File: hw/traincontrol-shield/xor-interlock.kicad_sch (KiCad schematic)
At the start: 4 parts, among them U3 74LVC1G86, U4 74LVC2G08

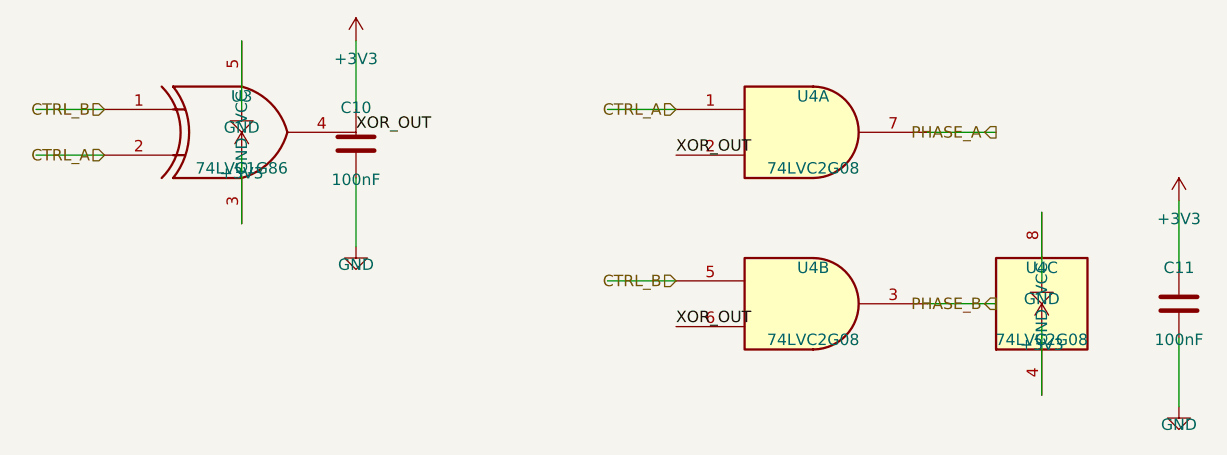
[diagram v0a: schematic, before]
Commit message: Revert "Fix hierarchical label orientations: angle=0 → angle=180 throughout"
This reverts commit 593a08d7401abe541600d63447176c71f07219f1.
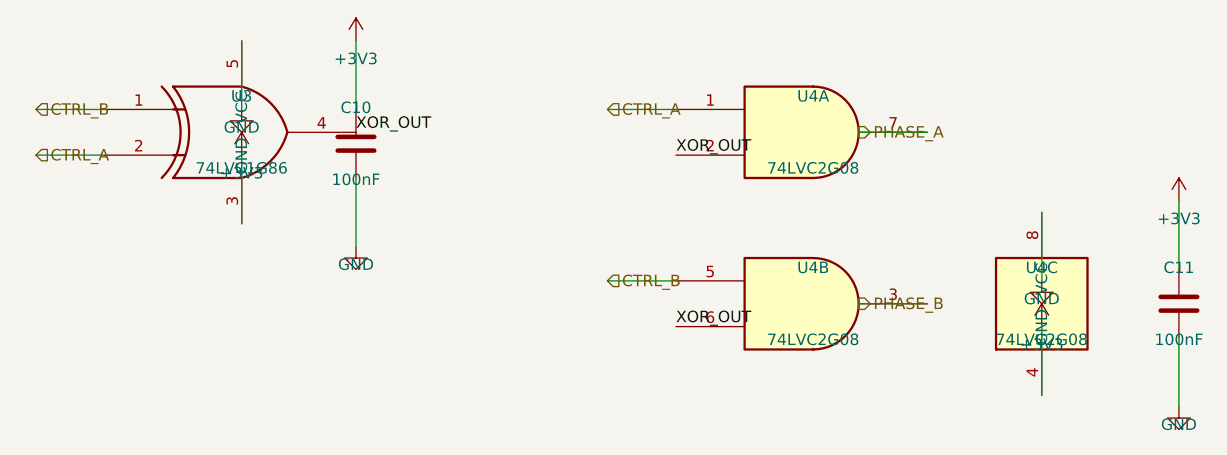
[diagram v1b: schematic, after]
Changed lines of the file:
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@@
 	(hierarchical_label "CTRL_A"
 		(shape input)
-		(at 48.26 92.71 180)
+		(at 40.64 92.71 0)
 		(fields_autoplaced yes)
-		(effects (font (size 1.27 1.27)) (justify right bottom))
+		(effects (font (size 1.27 1.27)) (justify left bottom))
 		(property "Intersheetrefs" "${INTERSHEET_REFS}"
-			(at 48.26 92.71 0)
+			(at 40.64 92.71 0)
 			(effects (font (size 1.27 1.27)) (hide yes))
 		)
@@
 	(hierarchical_label "CTRL_B"
 		(shape input)
-		(at 48.26 87.63 180)
+		(at 40.64 87.63 0)
 		(fields_autoplaced yes)
-		(effects (font (size 1.27 1.27)) (justify right bottom))
+		(effects (font (size 1.27 1.27)) (justify left bottom))
 		(property "Intersheetrefs" "${INTERSHEET_REFS}"
-			(at 48.26 87.63 0)
+			(at 40.64 87.63 0)
 			(effects (font (size 1.27 1.27)) (hide yes))
 		)
@@
 	(hierarchical_label "CTRL_A"
 		(shape input)
-		(at 111.76 87.63 180)
+		(at 104.14 87.63 0)
 		(fields_autoplaced yes)
-		(effects (font (size 1.27 1.27)) (justify right bottom))
+		(effects (font (size 1.27 1.27)) (justify left bottom))
 		(property "Intersheetrefs" "${INTERSHEET_REFS}"
-			(at 111.76 87.63 0)
+			(at 104.14 87.63 0)
 			(effects (font (size 1.27 1.27)) (hide yes))
 		)
@@
 	(hierarchical_label "CTRL_B"
 		(shape input)
-		(at 111.76 106.68 180)
+		(at 104.14 106.68 0)
 		(fields_autoplaced yes)
-		(effects (font (size 1.27 1.27)) (justify right bottom))
+		(effects (font (size 1.27 1.27)) (justify left bottom))
 		(property "Intersheetrefs" "${INTERSHEET_REFS}"
-			(at 111.76 106.68 0)
+			(at 104.14 106.68 0)
 			(effects (font (size 1.27 1.27)) (hide yes))
 		)
 	)
 	(wire
-		(pts (xy 139.7 90.17) (xy 147.32 90.17))
+		(pts (xy 132.07999999999998 90.17) (xy 139.7 90.17))
 		(stroke (width 0) (type solid))
 	)
 	(hierarchical_label "PHASE_A"
 		(shape output)
-		(at 147.32 90.17 180)
+		(at 132.07999999999998 90.17 0)
 		(fields_autoplaced yes)
-		(effects (font (size 1.27 1.27)) (justify right bottom))
+		(effects (font (size 1.27 1.27)) (justify left bottom))
 		(property "Intersheetrefs" "${INTERSHEET_REFS}"
-			(at 147.32 90.17 0)
+			(at 132.07999999999998 90.17 0)
 			(effects (font (size 1.27 1.27)) (hide yes))
 		)
 	)
 	(wire
-		(pts (xy 139.7 109.22) (xy 147.32 109.22))
+		(pts (xy 132.07999999999998 109.22) (xy 139.7 109.22))
 		(stroke (width 0) (type solid))
 	)
 	(hierarchical_label "PHASE_B"
 		(shape output)
-		(at 147.32 109.22 180)
+		(at 132.07999999999998 109.22 0)
 		(fields_autoplaced yes)
-		(effects (font (size 1.27 1.27)) (justify right bottom))
+		(effects (font (size 1.27 1.27)) (justify left bottom))
 		(property "Intersheetrefs" "${INTERSHEET_REFS}"
-			(at 147.32 109.22 0)
+			(at 132.07999999999998 109.22 0)
 			(effects (font (size 1.27 1.27)) (hide yes))
 		)
